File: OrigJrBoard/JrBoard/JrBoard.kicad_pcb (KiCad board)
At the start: 2 copper layers, 247 x 132 mm, 0 parts

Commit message: PCB work
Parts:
- added A1: 6532, Package_DIP:DIP-40_W15.24mm, F.Cu at (132.0, 104.8)
- added A2: 6507, Package_DIP:DIP-28_W15.24mm, F.Cu at (157.4, 111.2)
- added A3: UM6526P1, Package_DIP:DIP-40_W15.24mm, F.Cu at (182.8, 132.8)
- added A4: 4050, Package_DIP:DIP-16_W7.62mm, F.Cu at (167.0, -116.8)
- added A5: LM3086N, Package_DIP:DIP-14_W7.62mm, F.Cu at (109.5, -43.1)
- added C1: 1n, Atari2600Jr:C_leg_small, F.Cu at (83.7, -20.6)
- added C10: 1n, Atari2600Jr:C_leg_small, F.Cu at (224.3, -108.5)
- added C11: 470p, Atari2600Jr:C_leg_small, F.Cu at (126.6, -37.3)
- added C12: 100n, Atari2600Jr:C_leg_small, F.Cu at (173.7, -57.5)
- added C13: 68n, Atari2600Jr:C_oval_big, F.Cu at (219.5, -68.1)
- added C14: 68n, Atari2600Jr:C_oval_big, F.Cu at (219.5, -61.9)
- added C15: 1n, Atari2600Jr:C_leg_small, F.Cu at (156.4, -45.2)
- added C16: 1n, Atari2600Jr:C_leg_small, F.Cu at (156.4, -52.5)
- added C17: 1n, Atari2600Jr:C_leg_small, F.Cu at (192.9, -103.6)
- added C18: 1n, Atari2600Jr:C_leg_small, F.Cu at (183.3, -94.5)
- added C19: 470p, Atari2600Jr:C_leg_small, F.Cu at (103.9, -17.0)
- added C2: 100n, Atari2600Jr:C_leg_small, F.Cu at (159.0, -62.5)
- added C20: 4u7, Atari2600Jr:CP_small, F.Cu at (244.0, -95.0)
- added C21: 100n, Atari2600Jr:C_leg_small, F.Cu at (103.9, -13.3)
- added C22: 100n, Atari2600Jr:C_leg_small, F.Cu at (126.6, -40.9)
- added C23: 1n, Atari2600Jr:C_leg_small, F.Cu at (140.7, -52.5)
- added C24: 1n, Atari2600Jr:C_leg_small, F.Cu at (142.3, -48.8)
- added C25: 1n, Atari2600Jr:C_leg_small, F.Cu at (158.0, -56.2)
- added C26: 2m2, Atari2600Jr:CP_big, F.Cu at (35.5, 78.8)
- added C27: 4u7, Atari2600Jr:CP_small, F.Cu at (244.0, -101.2)
- added C28: 100n, Atari2600Jr:C_leg_small, F.Cu at (140.7, -45.2)
- added C29: 4u7, Atari2600Jr:CP_small, F.Cu at (243.2, -88.8)
- added C3: 1n, Atari2600Jr:C_leg_small, F.Cu at (115.1, -20.6)
- added C30: 39p, Atari2600Jr:C_oval_small, F.Cu at (117.0, -48.3)
- added C31: DNF, Atari2600Jr:C_oval_small, F.Cu at (117.7, -76.7)
- added C32: 18p, Atari2600Jr:C_4hole, F.Cu at (126.6, -33.6)
- added C33: 100p, Atari2600Jr:C_leg_small, F.Cu at (142.3, -41.5)
- added C34: 1n, Atari2600Jr:C_leg_small, F.Cu at (142.3, -37.9)
- added C35: 68p, Atari2600Jr:C_leg_small, F.Cu at (99.4, -20.6)
- added C36: 100n, Atari2600Jr:C_leg_small, F.Cu at (211.1, -117.1)
- added C37: 4u7, Atari2600Jr:CP_small, F.Cu at (179.5, -19.1)
- added C38: 100n, Atari2600Jr:C_leg_small, F.Cu at (208.6, -103.6)
- added C39: 10n, Atari2600Jr:C_leg_small, F.Cu at (208.6, -107.2)
- added C4: 1n, Atari2600Jr:C_leg_small, F.Cu at (140.7, -56.2)
- added C40: 10p, Atari2600Jr:C_leg_small, F.Cu at (208.6, -110.9)
- added C41: 100n, Atari2600Jr:C_leg_small, F.Cu at (183.3, -79.9)
- added C43: 100n, Atari2600Jr:C_leg_small, F.Cu at (183.3, -83.5)
- added C46: 56p, Atari2600Jr:C_leg_small, F.Cu at (183.3, -87.2)
- added C47: 100n, Atari2600Jr:C_leg_small, F.Cu at (199.0, -90.9)
- added C48: 820p, Atari2600Jr:C_leg_big, F.Cu at (64.8, -14.5)
- added C49: 100n, Atari2600Jr:C_leg_small, F.Cu at (199.8, -99.9)
- added C5: 68n, Atari2600Jr:C_oval_big, F.Cu at (202.9, -45.1)
- added C50: 47n, Atari2600Jr:C_leg_small, F.Cu at (183.3, -90.9)
- added C51: 22p, Atari2600Jr:C_leg_small, F.Cu at (199.0, -94.5)
- added C52: 47p, Atari2600Jr:C_leg_small, F.Cu at (119.6, -13.3)
- added C53: 820p, Atari2600Jr:C_leg_big, F.Cu at (101.6, -48.3)
- added C54: 820p, Atari2600Jr:C_leg_big, F.Cu at (85.6, -14.5)
- added C55: 22p, Atari2600Jr:C_leg_small, F.Cu at (119.6, -17.0)
- added C6: 68n, Atari2600Jr:C_oval_big, F.Cu at (180.2, -25.3)
- added C7: 1n, Atari2600Jr:C_leg_small, F.Cu at (226.8, -117.1)
- added C8: 1n, Atari2600Jr:C_leg_small, F.Cu at (172.1, -52.5)
- added C9: 1n, Atari2600Jr:C_leg_small, F.Cu at (158.0, -41.5)
- added CR2: 1N4148, Atari2600Jr:Diode, F.Cu at (126.6, -26.3)
- added CR3: 1N4148, Atari2600Jr:Diode, F.Cu at (199.0, -82.3)
- added CR4: 1N4148, Atari2600Jr:Diode, F.Cu at (130.8, -22.6)
- added CR5: 1N4148, Atari2600Jr:Diode, F.Cu at (142.3, -29.3)
- added DS1: LED RED, LED_THT:LED_D5.0mm_Clear, F.Cu at (213.8, -54.7)
- added J1: Joy left, Atari2600Jr:Joystick_conn, F.Cu at (70.3, -29.4)
- added J2: DC In, Atari2600Jr:DC_IN, F.Cu at (180.6, -109.5)
- added J3: Joy right, Atari2600Jr:Joystick_conn, F.Cu at (107.1, -53.3)
- added J4: RF_Out, Atari2600Jr:RF_Out, F.Cu at (173.6, -67.4)
- added J5: Cartridge Connector, Atari2600Jr:Cartridge, F.Cu at (149.8, 74.4)
- added J6: SEL / RES, Atari2600Jr:Button_conn, F.Cu at (138.2, -85.5)
- added L1: 1u, Atari2600Jr:L_small, F.Cu at (199.0, -86.6)
- added L11: 1u, Atari2600Jr:L_small, F.Cu at (142.3, -33.6)
- added L2: 1u, Atari2600Jr:L_small, F.Cu at (174.7, -61.8)
- added L3: 15u, Atari2600Jr:L_big, F.Cu at (194.1, -115.8)
- added L4: 1u, Atari2600Jr:L_small, F.Cu at (215.5, -99.3)
- added L5: 1u, Atari2600Jr:L_small, F.Cu at (224.3, -112.8)
- added L6: 0..1u, Atari2600Jr:L_var_2pin, F.Cu at (165.7, -15.3)
- added L7: 1u, Atari2600Jr:L_small, F.Cu at (189.6, -75.6)
- added L8: 0..4u, Atari2600Jr:L_var_5pin, F.Cu at (189.1, -34.0)
- added L9: 1u5, Atari2600Jr:L_big, F.Cu at (142.0, -61.1)
- added Q1: 2N3906, Package_TO_SOT_THT:TO-92, F.Cu at (243.8, -82.4)
- added Q2: 2N3906, Package_TO_SOT_THT:TO-92, F.Cu at (227.2, -64.8)
- added Q3: 2N3906, Package_TO_SOT_THT:TO-92, F.Cu at (174.6, -12.8)
- added Q4: 2N3904, Package_TO_SOT_THT:TO-92, F.Cu at (187.8, -25.1)
- added Q5: 2N3904, Package_TO_SOT_THT:TO-92, F.Cu at (198.7, -36.4)
- added R1: 1K8, Atari2600Jr:R0.5Inch, F.Cu at (158.0, -37.9)
- added R10: 220, Atari2600Jr:R0.5Inch, F.Cu at (173.7, -48.8)
- added R11: 240, Atari2600Jr:R0.5Inch, F.Cu at (146.5, -25.6)
- added R12: 100, Atari2600Jr:R0.5Inch, F.Cu at (205.3, -78.6)
- added R14: 3K3, Atari2600Jr:R0.5Inch, F.Cu at (172.1, -45.2)
- added R15: 10K, Atari2600Jr:R0.5Inch, F.Cu at (214.7, -87.7)
- added R16: 2K7, Atari2600Jr:R0.5Inch, F.Cu at (158.0, -30.5)
- added R17: 330, Atari2600Jr:R0.5Inch, F.Cu at (190.4, -64.0)
- added R18: 100, Atari2600Jr:R0.5Inch, F.Cu at (205.3, -71.3)
- added R19: 100, Atari2600Jr:R0.5Inch, F.Cu at (231.2, -101.2)
- added R2: 1K8, Atari2600Jr:R0.5Inch, F.Cu at (135.3, -15.3)
- added R20: 1K, Atari2600Jr:R0.5Inch, F.Cu at (240.0, -109.8)
- added R21: 1K5, Atari2600Jr:R0.5Inch, F.Cu at (190.4, -60.3)
- added R22: 4K7, Atari2600Jr:R0.5Inch, F.Cu at (214.7, -84.0)
- added R23: 91, Atari2600Jr:R0.5Inch, F.Cu at (205.3, -75.0)
- added R24: 1K, Atari2600Jr:R0.5Inch, F.Cu at (151.0, -21.9)
- added R25: 2K2, Atari2600Jr:R0.5Inch, F.Cu at (173.7, -41.5)
- added R26: 220, Atari2600Jr:R0.5Inch, F.Cu at (187.8, -53.9)
- added R27: 100, Atari2600Jr:R0.5Inch, F.Cu at (240.0, -113.4)
- added R28: 1M, Atari2600Jr:R0.5Inch, F.Cu at (126.6, -29.9)
- added R29: 1K, Atari2600Jr:R0.5Inch, F.Cu at (240.0, -106.1)
- added R3: 220, Atari2600Jr:R0.5Inch, F.Cu at (158.0, -34.2)
- added R30: 3K3, Atari2600Jr:R0.5Inch, F.Cu at (231.2, -97.5)
- added R31: 10K, Atari2600Jr:R0.5Inch, F.Cu at (173.7, -37.9)
- added R32: 100, Atari2600Jr:R0.5Inch, F.Cu at (173.7, -34.2)
- added R33: 3K3, Atari2600Jr:R0.5Inch, F.Cu at (230.4, -93.9)
- added R34: 1K, Atari2600Jr:R0.5Inch, F.Cu at (205.3, -67.6)
- added R35: 3K3, Atari2600Jr:R0.5Inch, F.Cu at (151.0, -14.6)
- added R36: 4K7, Atari2600Jr:R0.5Inch, F.Cu at (214.7, -95.0)
- added R37: 470, Atari2600Jr:R0.5Inch, F.Cu at (189.6, -71.3)
- added R38: 12K, Atari2600Jr:R0.5Inch, F.Cu at (224.3, -104.8)
- added R39: 4K7, Atari2600Jr:R0.5Inch, F.Cu at (230.4, -90.2)
- added R4: 10K, Atari2600Jr:R0.5Inch, F.Cu at (135.3, -11.6)
- added R40: 100K, Atari2600Jr:R0.5Inch, F.Cu at (221.0, -80.3)
- added R41: 3K3, Atari2600Jr:R0.5Inch, F.Cu at (206.1, -64.0)
- added R42: 6K8, Atari2600Jr:R0.5Inch, F.Cu at (187.8, -45.2)
- added R43: 9K1, Atari2600Jr:R0.5Inch, F.Cu at (173.7, -30.5)
- added R44: 6K8, Atari2600Jr:R0.5Inch, F.Cu at (162.2, -26.9)
- added R45: 10K, Atari2600Jr:R0.5Inch, F.Cu at (230.4, -86.5)
- added R46: 1K, Atari2600Jr:R0.5Inch, F.Cu at (166.7, -23.2)
- added R47: 100, Atari2600Jr:R0.5Inch, F.Cu at (206.1, -60.3)
- added R48: 18K, Atari2600Jr:R0.5Inch, F.Cu at (189.4, -50.2)
- added R49: 20K, Atari2600Jr:R0.5Inch, F.Cu at (189.4, -41.5)
- added R5: 1K8, Atari2600Jr:R0.5Inch, F.Cu at (189.6, -67.6)
- added R50: DNF, Atari2600Jr:R0.5Inch, F.Cu at (166.7, -19.6)
- added R51: 10K, Atari2600Jr:R0.5Inch, F.Cu at (203.5, -56.7)
- added R52: 39K, Atari2600Jr:R0.5Inch, F.Cu at (151.0, -18.3)
- added R53: 10K, Atari2600Jr:R0.5Inch, F.Cu at (221.0, -73.0)
- added R54: DNF, Atari2600Jr:R0.5Inch, F.Cu at (192.9, -110.9)
- added R55: 6K8, Atari2600Jr:R0.5Inch, F.Cu at (184.1, -98.2)
- added R56: 1K8, Atari2600Jr:R0.5Inch, F.Cu at (192.9, -107.2)
- added R57: 750, Atari2600Jr:R0.5Inch, F.Cu at (221.0, -76.7)
- added R6: 1K8, Atari2600Jr:R0.5Inch, F.Cu at (158.0, -48.8)
- added R7: 10K, Atari2600Jr:R0.5Inch, F.Cu at (135.3, -19.0)
- added R8: 220, Atari2600Jr:R0.5Inch, F.Cu at (214.7, -91.3)
- added R9: 500K, Atari2600Jr:R_Var, F.Cu at (98.7, -32.6)
- added S1: CH3/4, Atari2600Jr:Switch_rear, F.Cu at (102.0, -75.5)
- added S2: DIFF_L, Atari2600Jr:Switch_rear, F.Cu at (65.2, -23.2)
- added S3: DIFF_R, Atari2600Jr:Switch_rear, F.Cu at (133.6, -69.8)
- added S4: POWER_SW, Atari2600Jr:Switch_top, F.Cu at (168.5, -86.3)
- added S5: COLOR_SW, Atari2600Jr:Switch_top, F.Cu at (126.0, -53.5)
- added T1: TV_Trans, Atari2600Jr:Atari_TV_Trans, F.Cu at (235.7, -73.0)
- added TP1: 5V, TestPoint:TestPoint_Plated_Hole_D2.0mm, F.Cu at (199.0, -31.6)
- added TP2: A1_RES, TestPoint:TestPoint_Plated_Hole_D2.0mm, F.Cu at (242.4, -75.7)
- added TP3: 3.54MHz, TestPoint:TestPoint_Plated_Hole_D2.0mm, F.Cu at (221.2, -56.5)
- added TP4: A2_RES, TestPoint:TestPoint_Plated_Hole_D2.0mm, F.Cu at (184.9, -19.9)
- added TP5: A/V, TestPoint:TestPoint_Plated_Hole_D2.0mm, F.Cu at (210.9, -45.9)
- added TP6: 4.43MHz, TestPoint:TestPoint_Plated_Hole_D2.0mm, F.Cu at (82.9, -25.3)
- added TP7: Audio, TestPoint:TestPoint_Plated_Hole_D2.0mm, F.Cu at (78.2, -25.3)
- added VR1: L7805, Package_TO_SOT_THT:TO-220-3_Horizontal_TabDown, F.Cu at (128.3, -76.0)
- added W1: DNF, Atari2600Jr:Wire, F.Cu at (151.0, -11.3)
- added W2: DNF, Atari2600Jr:Wire, F.Cu at (114.8, -68.3)
- added W3: DNF, Atari2600Jr:Wire, F.Cu at (99.1, -68.3)
- added Y1: 3.546894MHz, Crystal:Crystal_HC18-U_Vertical, F.Cu at (232.9, -81.4)
- added Y2: 4.433618MHz, Crystal:Crystal_HC18-U_Vertical, F.Cu at (201.3, -51.5)
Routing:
- net /D5: track 0.00 -> 6.35 mm
- net /D4: track 0.00 -> 6.35 mm
- net /D3: track 0.00 -> 6.35 mm
- net /D2: track 0.00 -> 6.35 mm
- net /D1: track 0.00 -> 6.35 mm
- net /D0: track 0.00 -> 6.35 mm
- net /A5: track 0.00 -> 6.35 mm
- net /A4: track 0.00 -> 6.35 mm
- net /A3: track 0.00 -> 6.35 mm
- net /A2: track 0.00 -> 6.35 mm
- net /A1: track 0.00 -> 6.35 mm
- net /A0: track 0.00 -> 6.35 mm
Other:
- outline, holes or cut-outs redrawn

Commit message: PCB work
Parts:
- moved TP7 249.1 mm to (257.8, 147.4)
- moved A4 244.8 mm to (214.6, 123.2), turned to 270 degrees
- moved C53 237.7 mm to (247.0, 139.8), turned to 270 degrees
- moved DS1 237.3 mm to (52.0, 118.8), turned to 90 degrees
- moved C54 228.8 mm to (254.6, 139.8), turned to 90 degrees
- moved VR1 213.0 mm to (54.6, 123.9), turned to 180 degrees
- moved C7 210.3 mm to (94.6, 46.4), turned to 270 degrees
- moved S4 198.5 mm to (50.1, 73.1)
- moved C10 196.0 mm to (104.1, 46.4), turned to 270 degrees
- moved J6 192.9 mm to (255.9, 67.4)
- moved A5 191.1 mm to (227.3, 107.4), turned to 180 degrees
- moved L8 169.5 mm to (250.8, 123.9)
- moved C17 154.9 mm to (231.7, 46.4), turned to 270 degrees
- moved C48 150.7 mm to (93.9, 133.4), turned to 90 degrees
- moved C18 150.1 mm to (234.9, 46.4), turned to 270 degrees
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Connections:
- S5 pad 3: /PB3 -> GND
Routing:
- net GND: track 0.00 -> 25.4 mm
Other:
- outline, holes or cut-outs redrawn

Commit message: PCB top mostly done
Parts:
- CR2: footprint Atari2600Jr:Diode -> Atari2600Jr:Diode_short
- Q1, Q2, Q3, Q4, Q5: footprint Package_TO_SOT_THT:TO-92 -> Atari2600Jr:TR_TO92
- R15, R16, R17, R18, R20, R21: footprint Atari2600Jr:R0.5Inch -> Atari2600Jr:R_small
- TP1, TP2, TP3, TP4, TP5, TP6, TP7: footprint TestPoint:TestPoint_Plated_Hole_D2.0mm -> TestPoint:TestPoint_Pad_D1.5mm
- moved C36 286.2 mm to (39.3, 111.8), turned to 270 degrees
- moved R27 280.1 mm to (125.7, 142.3), turned to 270 degrees
- moved R45 273.1 mm to (81.2, 142.3), turned to 90 degrees
- moved R36 258.6 mm to (111.7, 142.3), turned to 90 degrees
- moved R38 256.6 mm to (111.7, 125.8), turned to 270 degrees
- moved C38 255.1 mm to (69.8, 110.5), turned to 270 degrees
- moved R56 252.9 mm to (234.3, 142.3), turned to 90 degrees
- moved R57 252.9 mm to (48.2, 108.0), turned to 90 degrees
- moved C47 252.5 mm to (102.2, 142.3), turned to 270 degrees
- moved R22 249.2 mm to (55.8, 108.0), turned to 270 degrees
- moved C39 248.2 mm to (89.5, 110.5), turned to 270 degrees
- moved C40 247.3 mm to (98.4, 110.5), turned to 270 degrees
- moved R39 244.9 mm to (114.9, 125.8), turned to 270 degrees
- moved R55 244.3 mm to (227.3, 142.3), turned to 270 degrees
- moved C27 241.5 mm to (111.1, 100.4), turned to 180 degrees
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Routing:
- net GND: track 25.4 -> 563.7 mm, vias 0 -> 13
- net /I2: track 0.00 -> 129.8 mm
- net /I3: track 0.00 -> 120.8 mm
- net /A12: track 0.00 -> 115.6 mm, vias 0 -> 2
- net /D6: track 0.00 -> 107.6 mm, vias 0 -> 1
- net /I4: track 0.00 -> 101.6 mm, vias 0 -> 1
- net /D7: track 0.00 -> 98.6 mm, vias 0 -> 2
- net +5V: track 0.00 -> 96.7 mm
- net VCC: track 0.00 -> 94.5 mm
- net /I0: track 0.00 -> 94.1 mm, vias 0 -> 1
- net /I1: track 0.00 -> 93.3 mm, vias 0 -> 1
- net /PB6: track 0.00 -> 89.6 mm, vias 0 -> 1
- net Net-(C4-Pad1): track 0.00 -> 88.8 mm, vias 0 -> 1
- net /A10: track 0.00 -> 84.9 mm
- net /A11: track 0.00 -> 80.9 mm
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- added copper zone on F.Cu, net GND
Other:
- outline, holes or cut-outs redrawn
- rule trace_min: 0.2 -> 0.127

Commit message: Finished PCB
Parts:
- TP1, TP2, TP3, TP4, TP5, TP6, TP7: footprint TestPoint:TestPoint_Pad_D1.5mm -> TestPoint:TestPoint_THTPad_D2.0mm_Drill1.0mm
- Y1: value 3.546894MHz -> 3.54MHz
- Y2: value 4.433618MHz -> 4.43MHz
- moved TP2 0.64 mm to (120.6, 88.3)
- moved TP4 0.64 mm to (218.4, 123.2)
- turned C48 to 270 degrees
- turned R17 to 180 degrees
- turned R37 to 270 degrees
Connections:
- R16 pad 2: GND -> Net-(C4-Pad1)
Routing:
- net GND: track 563.7 -> 1135.0 mm, vias 13 -> 89
- net Net-(A1-Pad20): track 48.4 -> 321.9 mm
- net Net-(C2-Pad1): track 5.70 -> 204.6 mm
- net Net-(C4-Pad1): track 88.8 -> 284.2 mm
- net /AUD: track 4.07 -> 150.2 mm
- net +5V: track 96.7 -> 238.8 mm
- net /I1: track 93.3 -> 224.8 mm
- net /I0: track 94.1 -> 224.4 mm
- net /PA0: track 0.00 -> 123.2 mm
- net /PA2: track 46.4 -> 166.3 mm
- net Net-(A3-Pad10): track 31.2 -> 150.0 mm
- net +5VA: track 59.9 -> 177.4 mm
- net /PB3: track 13.9 -> 121.1 mm
- net /I5: track 69.1 -> 176.1 mm
- net /PA1: track 40.0 -> 140.9 mm
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- added copper zone on B.Cu, net GND
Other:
- outline, holes or cut-outs redrawn

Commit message: Added Gerber files, going to production
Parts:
- added H1: MountingHole, Atari2600Jr:HoleEdge, F.Cu at (35.1, 141.7)
- added H2: MountingHole, Atari2600Jr:HoleEdge, F.Cu at (35.1, 39.7)
- added H3: MountingHole, Atari2600Jr:HoleTop, F.Cu at (159.6, 30.3)
- added H4: MountingHole, Atari2600Jr:HoleEdge, F.Cu at (263.7, 39.7)
- Y1: value 3.54MHz -> 3.546894MHz
- Y2: value 4.43MHz -> 4.433618MHz
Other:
- outline, holes or cut-outs redrawn

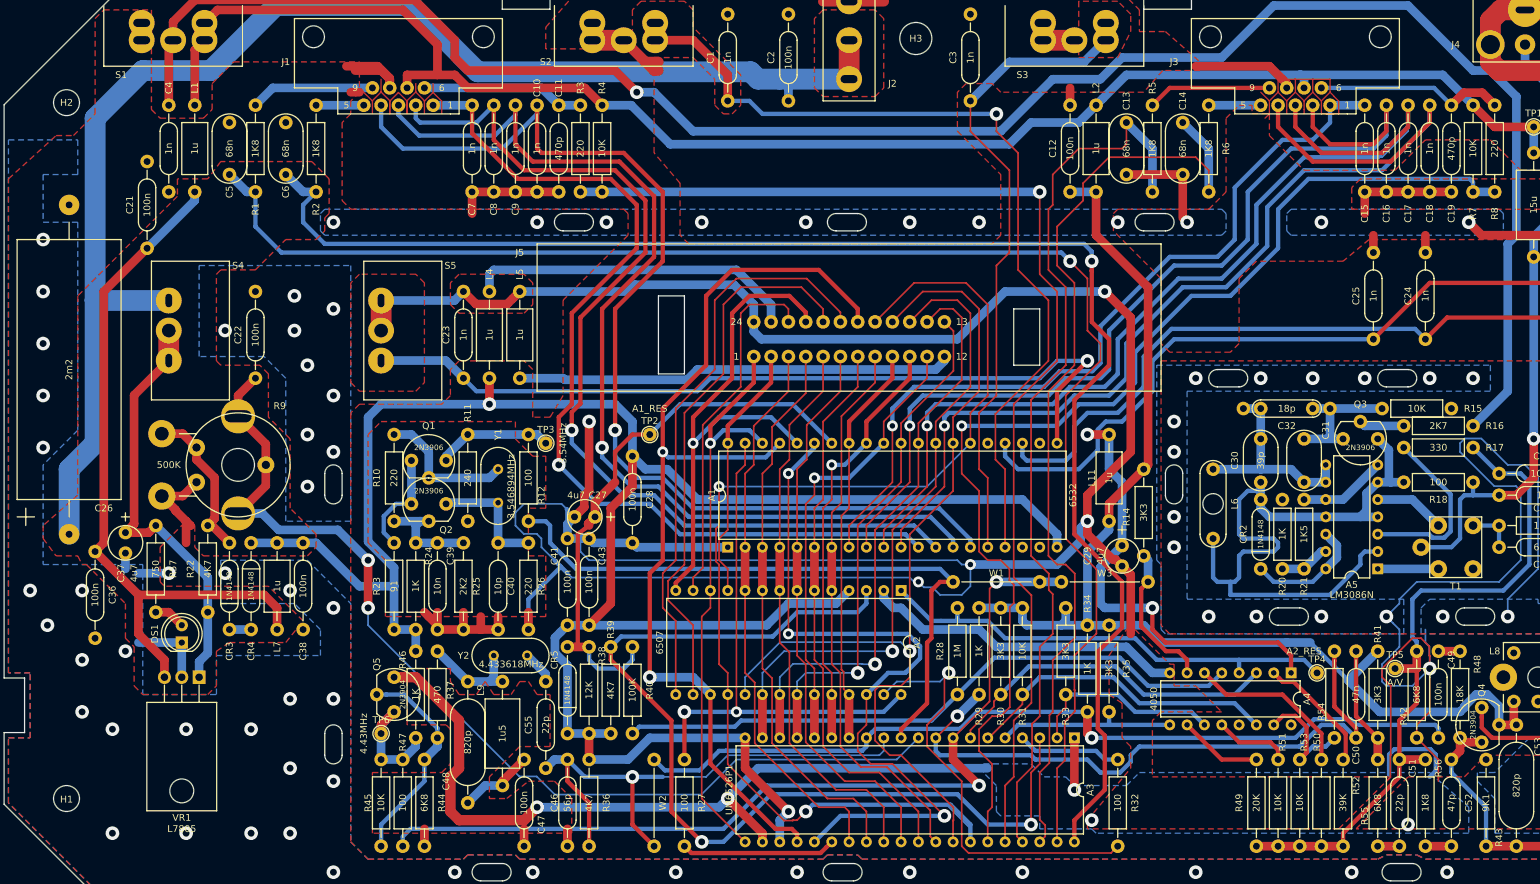
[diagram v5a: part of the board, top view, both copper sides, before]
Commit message: Corrections after first production
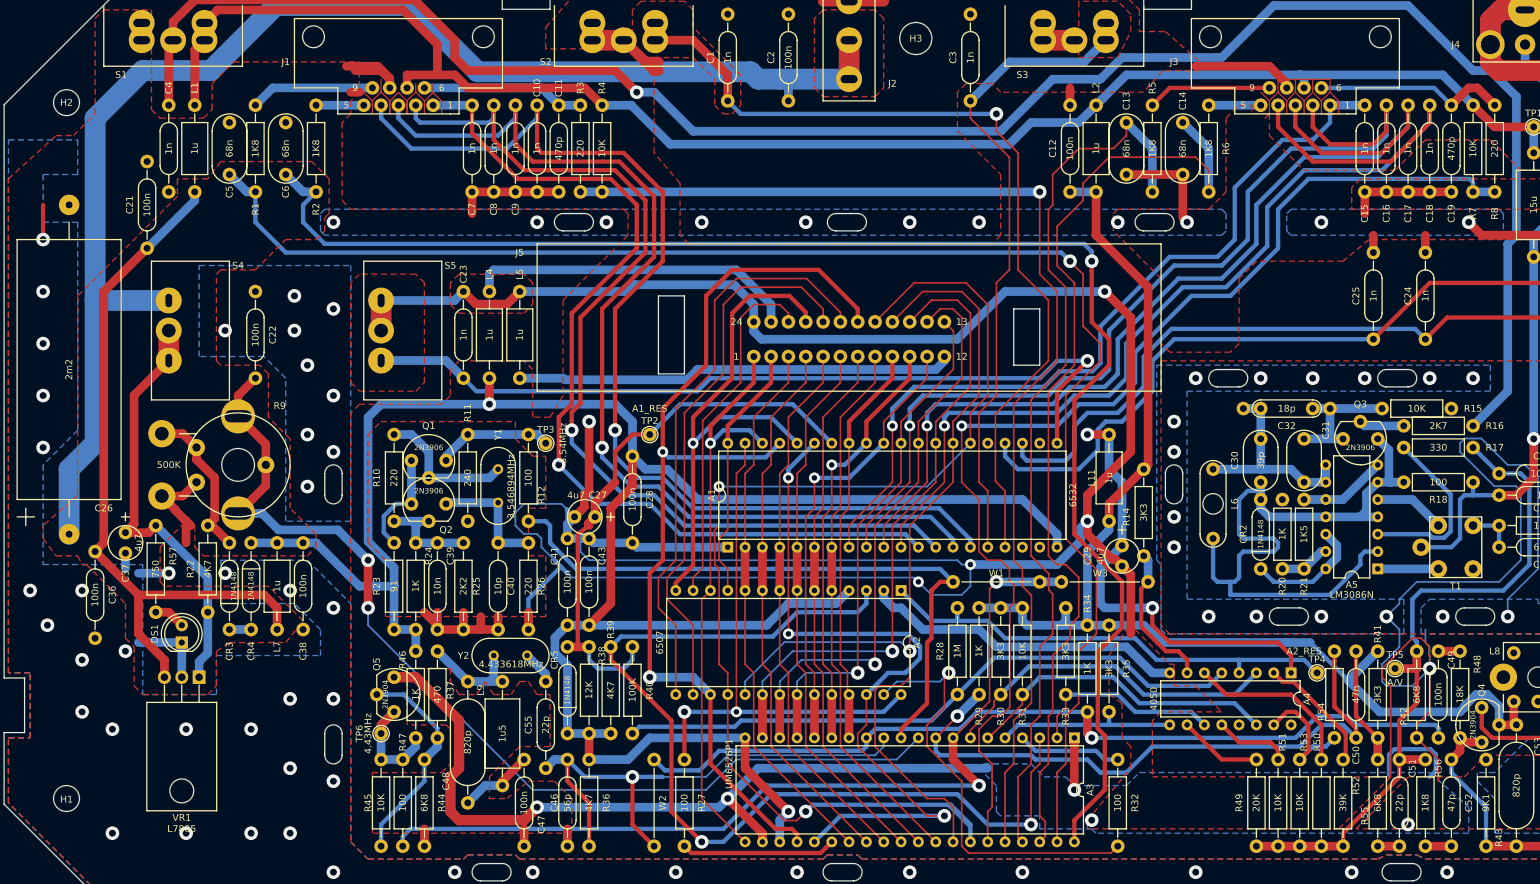
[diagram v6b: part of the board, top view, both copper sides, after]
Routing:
- net /PA2: track 166.3 -> 145.7 mm
- net GND: track 1135.0 -> 1140.1 mm
- net /A3: track 82.7 -> 80.1 mm
- net /A2: track 82.7 -> 80.1 mm
- net /A1: track 82.7 -> 80.1 mm
- net /A0: track 82.3 -> 80.1 mm
- net /A5: track 82.3 -> 80.1 mm
- net /A4: track 82.3 -> 80.1 mm
- net /PA5: track 145.3 -> 146.4 mm
- net Net-(A4-Pad15): track 17.6 -> 18.7 mm
- net /I3: track 132.6 -> 131.7 mm
- net /A8: track 53.2 -> 52.5 mm
- net /D5: track 95.1 -> 94.4 mm
- net Net-(A4-Pad6): track 24.6 -> 25.4 mm
- net Net-(C19-Pad1): track 28.0 -> 28.6 mm
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
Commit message: PCB corrections
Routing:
- net GND: track 1140.1 -> 1104.3 mm
- net +5V: track 238.8 -> 240.2 mm
- net /PA3: track 152.0 -> 153.0 mm
- net /PA4: track 138.8 -> 138.3 mm
- net Net-(J3-Pad5): track 7.62 -> 7.10 mm
- net Net-(J1-Pad5): track 6.98 -> 6.47 mm
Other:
- outline, holes or cut-outs redrawn
